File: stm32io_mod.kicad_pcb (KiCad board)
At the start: 2 copper layers, 70.5 x 73.7 mm, 53 parts, among them J1 UART, M1 BluePill, Q1 BC858, Q2 BC858, Q3 BC858, Q4 BC858, SW1 button_1, SW2 button_2, SW3 button_3, SW4 button_4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

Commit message: Se añade licencia
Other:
- board text added: "MIT License Copyright (c) 2020 Matías S. Ávalos (msavalos@gmail.com) Permission is hereby granted, free of charge, to any person obtaining a copy of this software and associated documentation files (the "Software"), to deal in the Software without restriction, including without limitation the rights to use, copy, modify, merge, publish, distribute, sublicense, and/or sell copies of the Software, 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"
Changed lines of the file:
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@@
   (general
     (thickness 1.6)
-    (drawings 4)
+    (drawings 5)
     (tracks 292)
     (zones 0)
@@
     )
   )
+  (gr_text "MIT License\n\nCopyright (c) 2020 Matías S. Ávalos (msavalos@gmail.com)\n\nPermission is hereby granted, free of charge, to any person obtaining a copy\nof this software and associated documentation files (the \"Software\"), to deal\nin the Software without restriction, including without limitation the rights\nto use, copy, modify, merge, publish, distribute, sublicense, and/or sell\ncopies of the Software, and to permit persons to whom the Software is\nfurnished to do so, subject to the following conditions:\n\nThe above copyright notice and this permission notice shall be included in all\ncopies or substantial portions of the Software.\n\nTHE SOFTWARE IS PROVIDED \"AS IS\", WITHOUT WARRANTY OF ANY KIND, EXPRESS OR\nIMPLIED, INCLUDING BUT NOT LIMITED TO THE WARRANTIES OF MERCHANTABILITY,\nFITNESS FOR A PARTICULAR PURPOSE AND NONINFRINGEMENT. IN NO EVENT SHALL THE\nAUTHORS OR COPYRIGHT HOLDERS BE LIABLE FOR ANY CLAIM, DAMAGES OR OTHER\nLIABILITY, WHETHER IN AN ACTION OF CONTRACT, TORT OR OTHERWISE, ARISING FROM,\nOUT OF OR IN CONNECTION WITH THE SOFTWARE OR THE USE OR OTHER DEALINGS IN THE\nSOFTWARE.\n" (at 12.065 -26.416) (layer Dwgs.User)
+    (effects (font (size 2 2) (thickness 0.4)) (justify left))
+  )
   (gr_line (start 109.855 58.42) (end 180.34 58.42) (layer Edge.Cuts) (width 0.3))

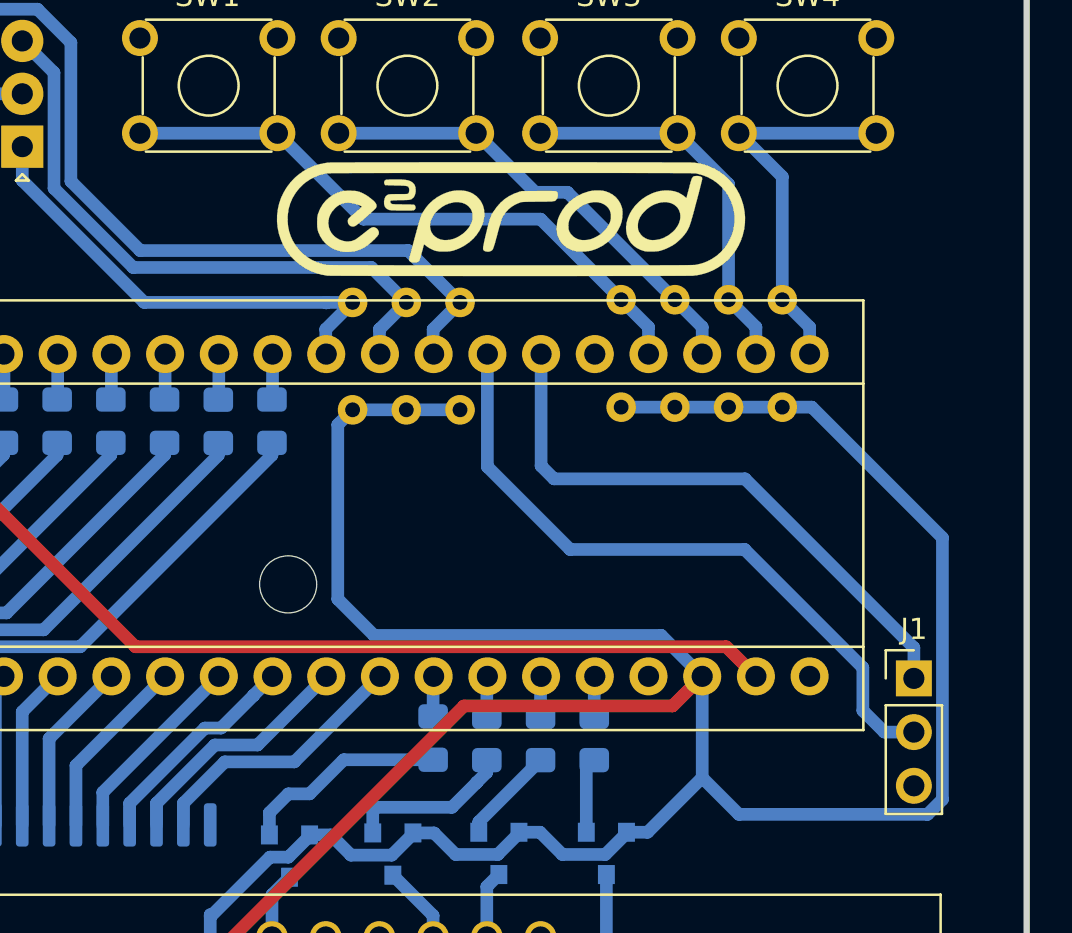
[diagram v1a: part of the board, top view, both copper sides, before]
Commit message: cambio de resistencias a smd
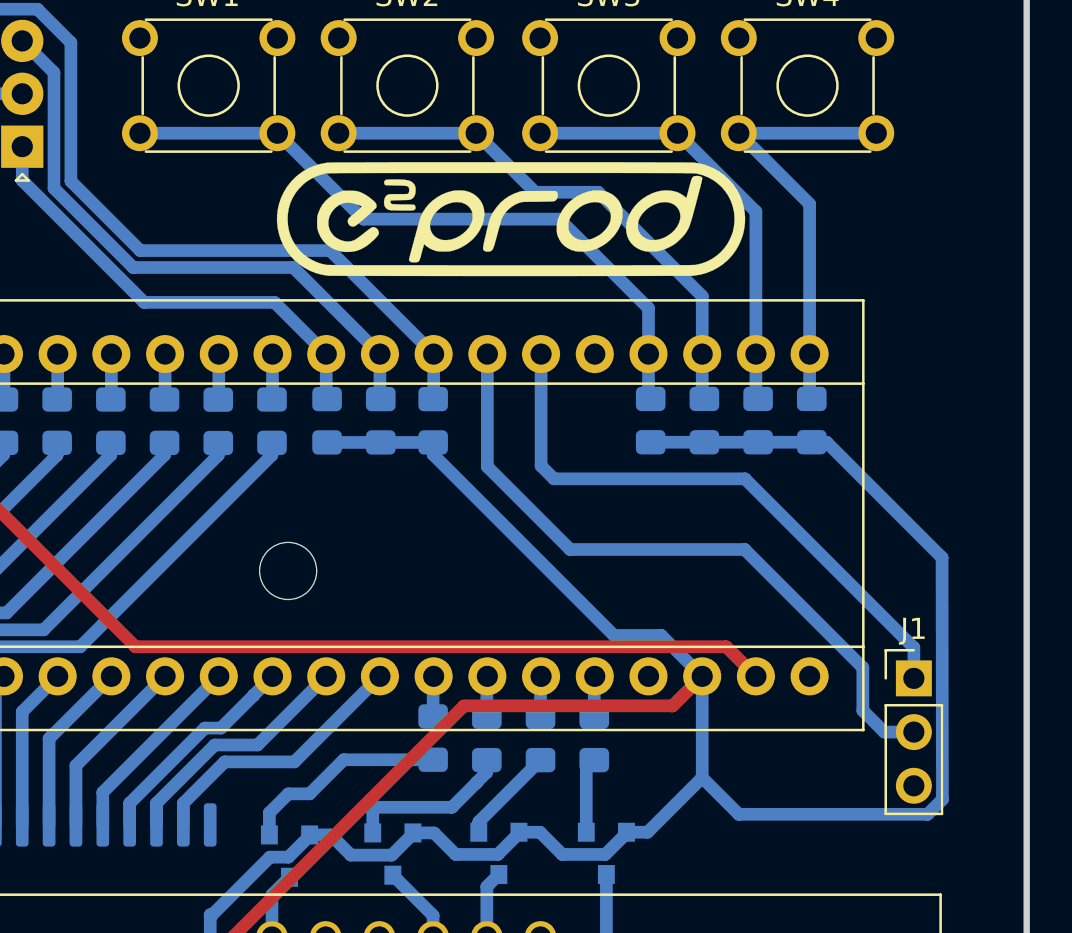
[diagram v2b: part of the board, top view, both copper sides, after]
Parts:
- D1: value LED_RGBC -> RGB
- R1, R11, R12, R13, R14, R16, R2: value R -> 10k; footprint Resistor_THT:R_Axial_DIN0204_L3.6mm_D1.6mm_P5.08mm_Horizontal -> Resistor_SMD:R_0805_2012Metric_Pad1.15x1.40mm_HandSolder
- R10, R3, R4, R5, R6, R7, R8, R9: value R -> 47Ω
- R17, R18, R19, R22, R23, R24, R25: value R -> 100Ω
- R20, R21, R26, R27: value R -> 2k7
- moved R12 5.88 mm to (170.2, 84.8)
- moved R1 5.88 mm to (162.6, 84.8)
- moved R11 5.88 mm to (165.1, 84.8)
- moved R2 5.88 mm to (167.6, 84.8)
- moved R13 5.73 mm to (147.3, 84.8)
- moved R16 1.37 mm to (152.3, 84.8)
- moved R14 1.31 mm to (149.8, 84.8)
- moved REF** 0.64 mm to (145.4, 91.9)
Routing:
- net VCC: track 233.5 -> 220.4 mm
- net sw2: track 22.3 -> 25.3 mm
- net sw1: track 29.1 -> 31.8 mm
- net sw4: track 18.3 -> 20.5 mm
- net sw3: track 18.5 -> 20.6 mm
- net rotA: track 22.6 -> 21.6 mm
- net swr: track 48.4 -> 47.3 mm
- net rotB: track 29.5 -> 28.4 mm

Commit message: Pequeños arreglos en el PCB
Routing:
- net VCC: track 220.4 -> 164.1 mm
- net GND: track 65.0 -> 15.5 mm
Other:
- board text added: "Rx"
- board text added: "Tx"
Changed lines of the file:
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@@
   (general
     (thickness 1.6)
-    (drawings 5)
-    (tracks 292)
+    (drawings 7)
+    (tracks 283)
     (zones 0)
     (modules 53)
@@
       (effects (font (size 1 1) (thickness 0.15)))
     )
-    (fp_text value UART (at 2.286 2.667 90) (layer F.Fab)
+    (fp_text value UART (at -2.4765 5.08 90) (layer F.Fab)
       (effects (font (size 1 1) (thickness 0.15)))
     )
@@
     )
   )
+  (gr_text Rx (at 177.673 99.568) (layer F.SilkS)
+    (effects (font (size 1.3 1.3) (thickness 0.2)))
+  )
+  (gr_text Tx (at 177.7365 97.028) (layer F.SilkS)
+    (effects (font (size 1.3 1.3) (thickness 0.2)))
+  )
   (gr_text "MIT License\n\nCopyright (c) 2020 Matías S. Ávalos (msavalos@gmail.com)\n\nPermission is hereby granted, free of charge, to any person obtaining a copy\nof this software and associated documentation files (the \"Software\"), to deal\nin the Software without restriction, including without limitation the rights\nto use, copy, modify, merge, publish, distribute, sublicense, and/or sell\ncopies of the Software, and to permit persons to whom the Software is\nfurnished to do so, subject to the following conditions:\n\nThe above copyright notice and this permission notice shall be included in all\ncopies or substantial portions of the Software.\n\nTHE SOFTWARE IS PROVIDED \"AS IS\", WITHOUT WARRANTY OF ANY KIND, EXPRESS OR\nIMPLIED, INCLUDING BUT NOT LIMITED TO THE WARRANTIES OF MERCHANTABILITY,\nFITNESS FOR A PARTICULAR PURPOSE AND NONINFRINGEMENT. IN NO EVENT SHALL THE\nAUTHORS OR COPYRIGHT HOLDERS BE LIABLE FOR ANY CLAIM, DAMAGES OR OTHER\nLIABILITY, WHETHER IN AN ACTION OF CONTRACT, TORT OR OTHERWISE, ARISING FROM,\nOUT OF OR IN CONNECTION WITH THE SOFTWARE OR THE USE OR OTHER DEALINGS IN THE\nSOFTWARE.\n" (at 12.065 -26.416) (layer Dwgs.User)
     (effects (font (size 2 2) (thickness 0.4)) (justify left))
@@
   (segment (start 149.731 109.258) (end 149.731 111.018) (width 0.6) (layer B.Cu) (net 7))
   (segment (start 154.811 122.72) (end 154.811 124.498) (width 0.6) (layer B.Cu) (net 8))
-  (segment (start 125.255999 82.591999) (end 124.356 81.692) (width 0.6) (layer F.Cu) (net 9))
-  (segment (start 138.195999 95.531999) (end 125.255999 82.591999) (width 0.6) (layer F.Cu) (net 9))
-  (segment (start 166.135999 95.531999) (end 138.195999 95.531999) (width 0.6) (layer F.Cu) (net 9))
-  (segment (start 167.536 96.932) (end 166.135999 95.531999) (width 0.6) (layer F.Cu) (net 9))
   (segment (start 120.842 69.382) (end 118.342 71.882) (width 0.6) (layer B.Cu) (net 9))
   (segment (start 132.842 69.382) (end 120.842 69.382) (width 0.6) (layer B.Cu) (net 9))
@@
   (segment (start 176.356001 102.756001) (end 175.654001 103.458001) (width 0.6) (layer B.Cu) (net 18))
   (segment (start 166.730001 103.458001) (end 164.996 101.724) (width 0.6) (layer B.Cu) (net 18))
-  (segment (start 164.096001 97.831999) (end 164.996 96.932) (width 0.6) (layer F.Cu) (net 18))
-  (segment (start 153.726997 98.332001) (end 163.595999 98.332001) (width 0.6) (layer F.Cu) (net 18))
-  (segment (start 163.595999 98.332001) (end 164.096001 97.831999) (width 0.6) (layer F.Cu) (net 18))
-  (segment (start 127.057098 125.0019) (end 153.726997 98.332001) (width 0.6) (layer F.Cu) (net 18))
-  (segment (start 120.2412 125.0019) (end 127.057098 125.0019) (width 0.6) (layer F.Cu) (net 18))
   (segment (start 112.580639 90.927361) (end 120.916001 82.591999) (width 0.6) (layer B.Cu) (net 18))
   (segment (start 112.580639 122.994639) (end 112.580639 90.927361) (width 0.6) (layer B.Cu) (net 18))

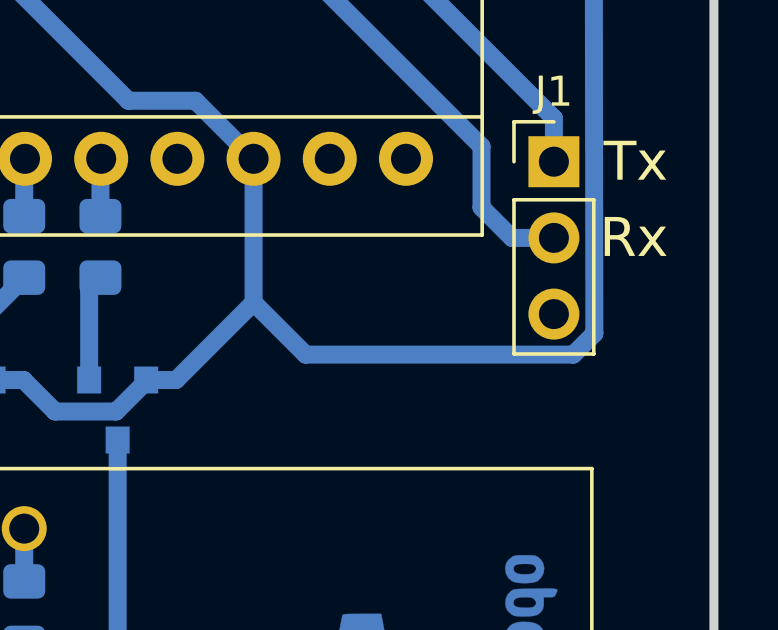
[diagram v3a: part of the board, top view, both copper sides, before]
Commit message: Agregado VCC al pinhead de la UART
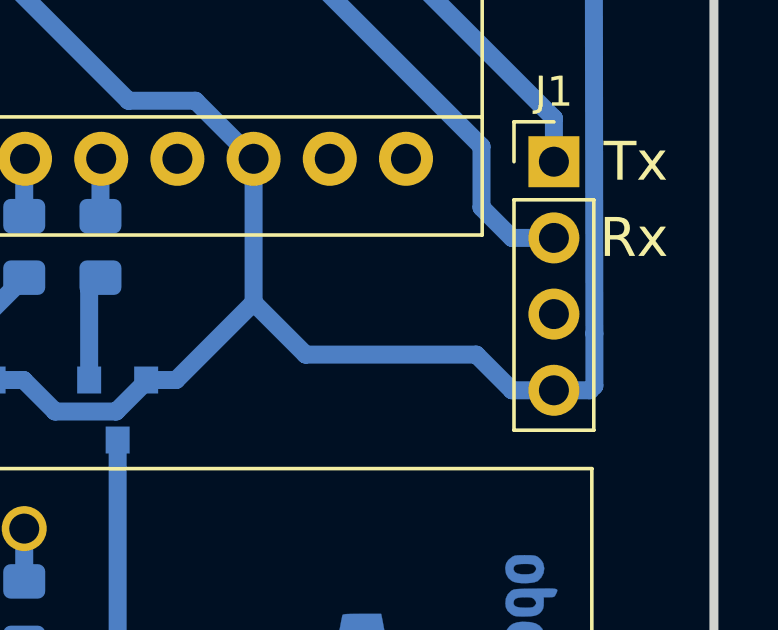
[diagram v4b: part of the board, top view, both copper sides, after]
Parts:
- J1: footprint Connector_PinHeader_2.54mm:PinHeader_1x03_P2.54mm_Vertical -> Connector_PinHeader_2.54mm:PinHeader_1x04_P2.54mm_Vertical
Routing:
- net VCC: track 164.1 -> 166.1 mm
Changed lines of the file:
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@@
     (thickness 1.6)
     (drawings 7)
-    (tracks 283)
+    (tracks 287)
     (zones 0)
     (modules 53)
@@
     (add_net swr)
   )
+  (module Connector_PinHeader_2.54mm:PinHeader_1x04_P2.54mm_Vertical (layer F.Cu)
+    (at 175.006 97.028)
+    (descr "Through hole straight pin header, 1x04, 2.54mm pitch, single row")
+    (tags "Through hole pin header THT 1x04 2.54mm single row")
+    (fp_text reference J1 (at 0 -2.33) (layer F.SilkS)
+      (effects (font (size 1 1) (thickness 0.15)))
+    )
+    (fp_text value UART (at 2.7305 7.4295 90) (layer F.Fab)
+      (effects (font (size 1 1) (thickness 0.15)))
+    )
+    (fp_text user %R (at 0 3.81 90) (layer F.Fab)
+      (effects (font (size 1 1) (thickness 0.15)))
+    )
+    (fp_line (start 1.8 -1.8) (end -1.8 -1.8) (layer F.CrtYd) (width 0.05))
+    (fp_line (start 1.8 9.4) (end 1.8 -1.8) (layer F.CrtYd) (width 0.05))
+    (fp_line (start -1.8 9.4) (end 1.8 9.4) (layer F.CrtYd) (width 0.05))
+    (fp_line (start -1.8 -1.8) (end -1.8 9.4) (layer F.CrtYd) (width 0.05))
+    (fp_line (start -1.33 -1.33) (end 0 -1.33) (layer F.SilkS) (width 0.12))
+    (fp_line (start -1.33 0) (end -1.33 -1.33) (layer F.SilkS) (width 0.12))
+    (fp_line (start -1.33 1.27) (end 1.33 1.27) (layer F.SilkS) (width 0.12))
+    (fp_line (start 1.33 1.27) (end 1.33 8.95) (layer F.SilkS) (width 0.12))
+    (fp_line (start -1.33 1.27) (end -1.33 8.95) (layer F.SilkS) (width 0.12))
+    (fp_line (start -1.33 8.95) (end 1.33 8.95) (layer F.SilkS) (width 0.12))
+    (fp_line (start -1.27 -0.635) (end -0.635 -1.27) (layer F.Fab) (width 0.1))
+    (fp_line (start -1.27 8.89) (end -1.27 -0.635) (layer F.Fab) (width 0.1))
+    (fp_line (start 1.27 8.89) (end -1.27 8.89) (layer F.Fab) (width 0.1))
+    (fp_line (start 1.27 -1.27) (end 1.27 8.89) (layer F.Fab) (width 0.1))
+    (fp_line (start -0.635 -1.27) (end 1.27 -1.27) (layer F.Fab) (width 0.1))
+    (pad 4 thru_hole oval (at 0 7.62) (size 1.7 1.7) (drill 1) (layers *.Cu *.Mask)
+      (net 18 VCC))
+    (pad 3 thru_hole oval (at 0 5.08) (size 1.7 1.7) (drill 1) (layers *.Cu *.Mask)
+      (net 9 GND))
+    (pad 2 thru_hole oval (at 0 2.54) (size 1.7 1.7) (drill 1) (layers *.Cu *.Mask)
+      (net 16 Rx))
+    (pad 1 thru_hole rect (at 0 0) (size 1.7 1.7) (drill 1) (layers *.Cu *.Mask)
+      (net 17 Tx))
+    (model ${KISYS3DMOD}/Connector_PinHeader_2.54mm.3dshapes/PinHeader_1x04_P2.54mm_Vertical.wrl
+      (at (xyz 0 0 0))
+      (scale (xyz 1 1 1))
+      (rotate (xyz 0 0 0))
+    )
+  )
   (module e2prod:e2prod-silks (layer F.Cu)
     (at 155.956 75.311)
@@
     )
   )
-  (module Connector_PinHeader_2.54mm:PinHeader_1x03_P2.54mm_Vertical (layer F.Cu)
-    (at 175.006 97.028)
-    (descr "Through hole straight pin header, 1x03, 2.54mm pitch, single row")
-    (tags "Through hole pin header THT 1x03 2.54mm single row")
-    (fp_text reference J1 (at 0 -2.33) (layer F.SilkS)
-      (effects (font (size 1 1) (thickness 0.15)))
-    )
-    (fp_text value UART (at -2.4765 5.08 90) (layer F.Fab)
-      (effects (font (size 1 1) (thickness 0.15)))
-    )
-    (fp_text user %R (at 0 -2.3368 180) (layer F.Fab)
-      (effects (font (size 1 1) (thickness 0.15)))
-    )
-    (fp_line (start 1.8 -1.8) (end -1.8 -1.8) (layer F.CrtYd) (width 0.05))
-    (fp_line (start 1.8 6.85) (end 1.8 -1.8) (layer F.CrtYd) (width 0.05))
-    (fp_line (start -1.8 6.85) (end 1.8 6.85) (layer F.CrtYd) (width 0.05))
-    (fp_line (start -1.8 -1.8) (end -1.8 6.85) (layer F.CrtYd) (width 0.05))
-    (fp_line (start -1.33 -1.33) (end 0 -1.33) (layer F.SilkS) (width 0.12))
-    (fp_line (start -1.33 0) (end -1.33 -1.33) (layer F.SilkS) (width 0.12))
-    (fp_line (start -1.33 1.27) (end 1.33 1.27) (layer F.SilkS) (width 0.12))
-    (fp_line (start 1.33 1.27) (end 1.33 6.41) (layer F.SilkS) (width 0.12))
-    (fp_line (start -1.33 1.27) (end -1.33 6.41) (layer F.SilkS) (width 0.12))
-    (fp_line (start -1.33 6.41) (end 1.33 6.41) (layer F.SilkS) (width 0.12))
-    (fp_line (start -1.27 -0.635) (end -0.635 -1.27) (layer F.Fab) (width 0.1))
-    (fp_line (start -1.27 6.35) (end -1.27 -0.635) (layer F.Fab) (width 0.1))
-    (fp_line (start 1.27 6.35) (end -1.27 6.35) (layer F.Fab) (width 0.1))
-    (fp_line (start 1.27 -1.27) (end 1.27 6.35) (layer F.Fab) (width 0.1))
-    (fp_line (start -0.635 -1.27) (end 1.27 -1.27) (layer F.Fab) (width 0.1))
-    (pad 3 thru_hole oval (at 0 5.08) (size 1.7 1.7) (drill 1) (layers *.Cu *.Mask)
-      (net 9 GND))
-    (pad 2 thru_hole oval (at 0 2.54) (size 1.7 1.7) (drill 1) (layers *.Cu *.Mask)
-      (net 16 Rx))
-    (pad 1 thru_hole rect (at 0 0) (size 1.7 1.7) (drill 1) (layers *.Cu *.Mask)
-      (net 17 Tx))
-    (model ${KISYS3DMOD}/Connector_PinHeader_2.54mm.3dshapes/PinHeader_1x03_P2.54mm_Vertical.wrl
-      (at (xyz 0 0 0))
-      (scale (xyz 1 1 1))
-      (rotate (xyz 0 0 0))
-    )
-  )
   (module LED_THT:LED_D3.0mm_Clear (layer F.Cu)
     (at 121.3207 105.1899 180)
@@
   (segment (start 141.732 108.204) (end 141.73 108.3055) (width 0.6) (layer B.Cu) (net 18))
   (segment (start 164.996 96.932) (end 163.06 94.996) (width 0.6) (layer B.Cu) (net 18))
-  (segment (start 175.654001 103.458001) (end 166.730001 103.458001) (width 0.6) (layer B.Cu) (net 18))
-  (segment (start 176.356001 102.756001) (end 175.654001 103.458001) (width 0.6) (layer B.Cu) (net 18))
   (segment (start 166.730001 103.458001) (end 164.996 101.724) (width 0.6) (layer B.Cu) (net 18))
   (segment (start 112.580639 90.927361) (end 120.916001 82.591999) (width 0.6) (layer B.Cu) (net 18))
@@
   (segment (start 170.88 85.861) (end 176.332 91.313) (width 0.6) (layer B.Cu) (net 18))
   (segment (start 176.3395 91.313) (end 176.356001 102.756001) (width 0.6) (layer B.Cu) (net 18))
+  (segment (start 166.730001 103.458001) (end 172.419001 103.458001) (width 0.6) (layer B.Cu) (net 18))
+  (segment (start 173.609 104.648) (end 175.006 104.648) (width 0.6) (layer B.Cu) (net 18))
+  (segment (start 172.419001 103.458001) (end 173.609 104.648) (width 0.6) (layer B.Cu) (net 18))
+  (segment (start 176.356001 104.50008) (end 176.356001 102.756001) (width 0.6) (layer B.Cu) (net 18))
+  (segment (start 176.208081 104.648) (end 176.356001 104.50008) (width 0.6) (layer B.Cu) (net 18))
+  (segment (start 175.006 104.648) (end 176.208081 104.648) (width 0.6) (layer B.Cu) (net 18))
   (segment (start 131.57 97.338) (end 131.976 96.932) (width 0.6) (layer B.Cu) (net 22))
   (segment (start 131.57 103.9585) (end 131.57 97.338) (width 0.6) (layer B.Cu) (net 22))
